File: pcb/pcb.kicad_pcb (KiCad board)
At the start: 2 copper layers, 156.4 x 127.2 mm, 67 parts, among them SW1 SW_Push, SW10 SW_Push, SW11 SW_Push, SW12 SW_Push, SW13 SW_Push, SW14 SW_Push, SW15 SW_Push, SW16 SW_Push, SW17 SW_Push, SW18 SW_Push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

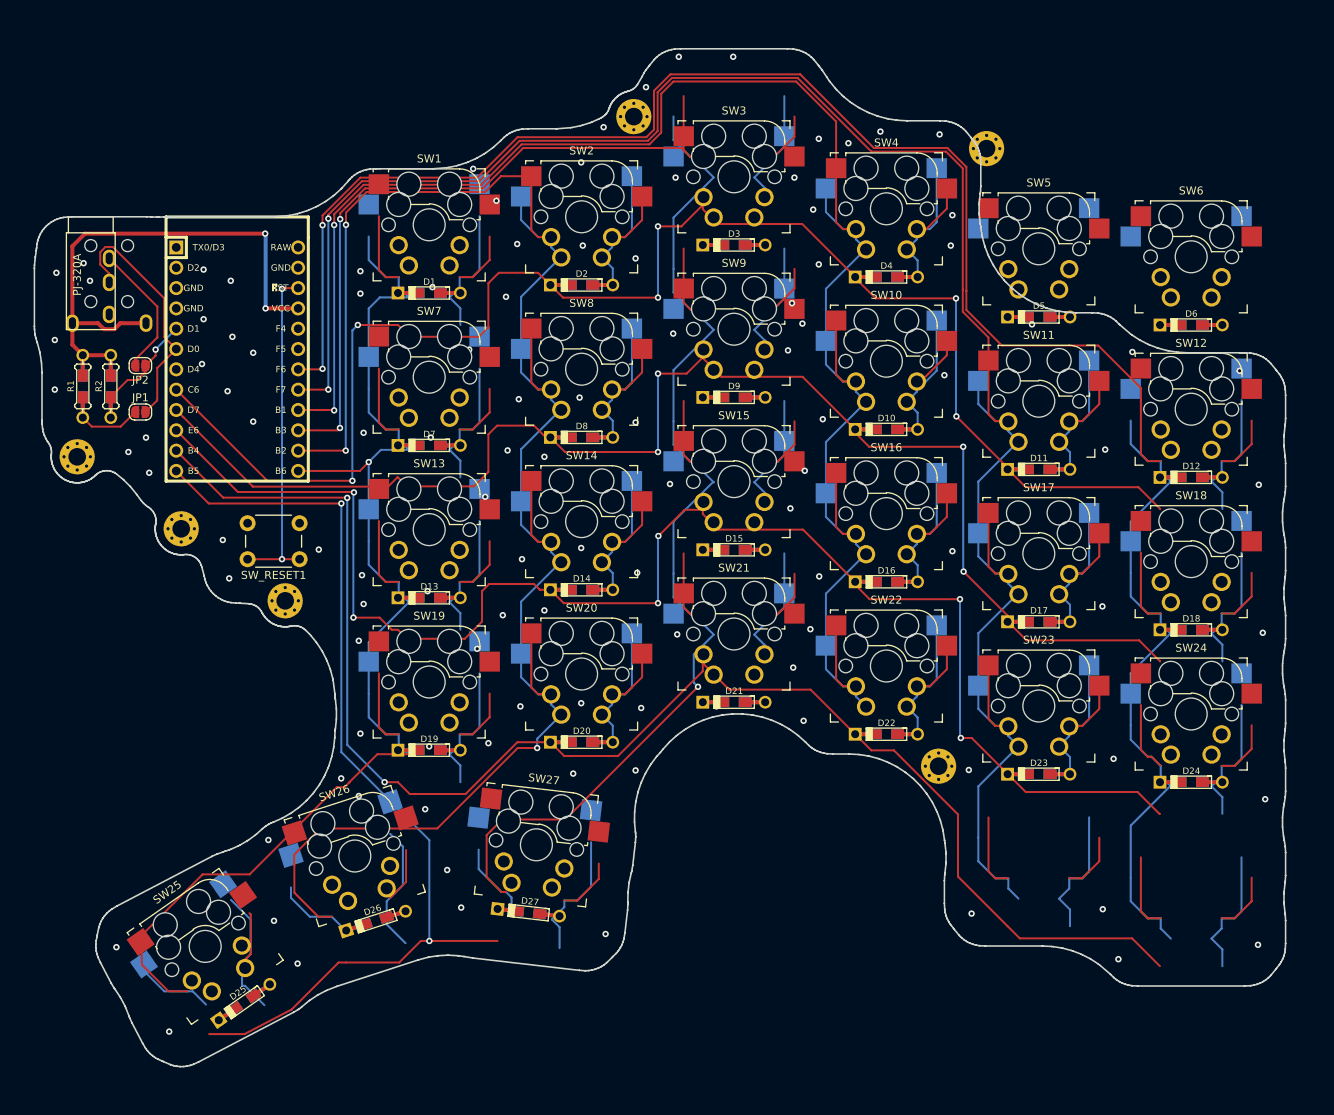
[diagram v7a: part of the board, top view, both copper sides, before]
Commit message: Route new switch placement
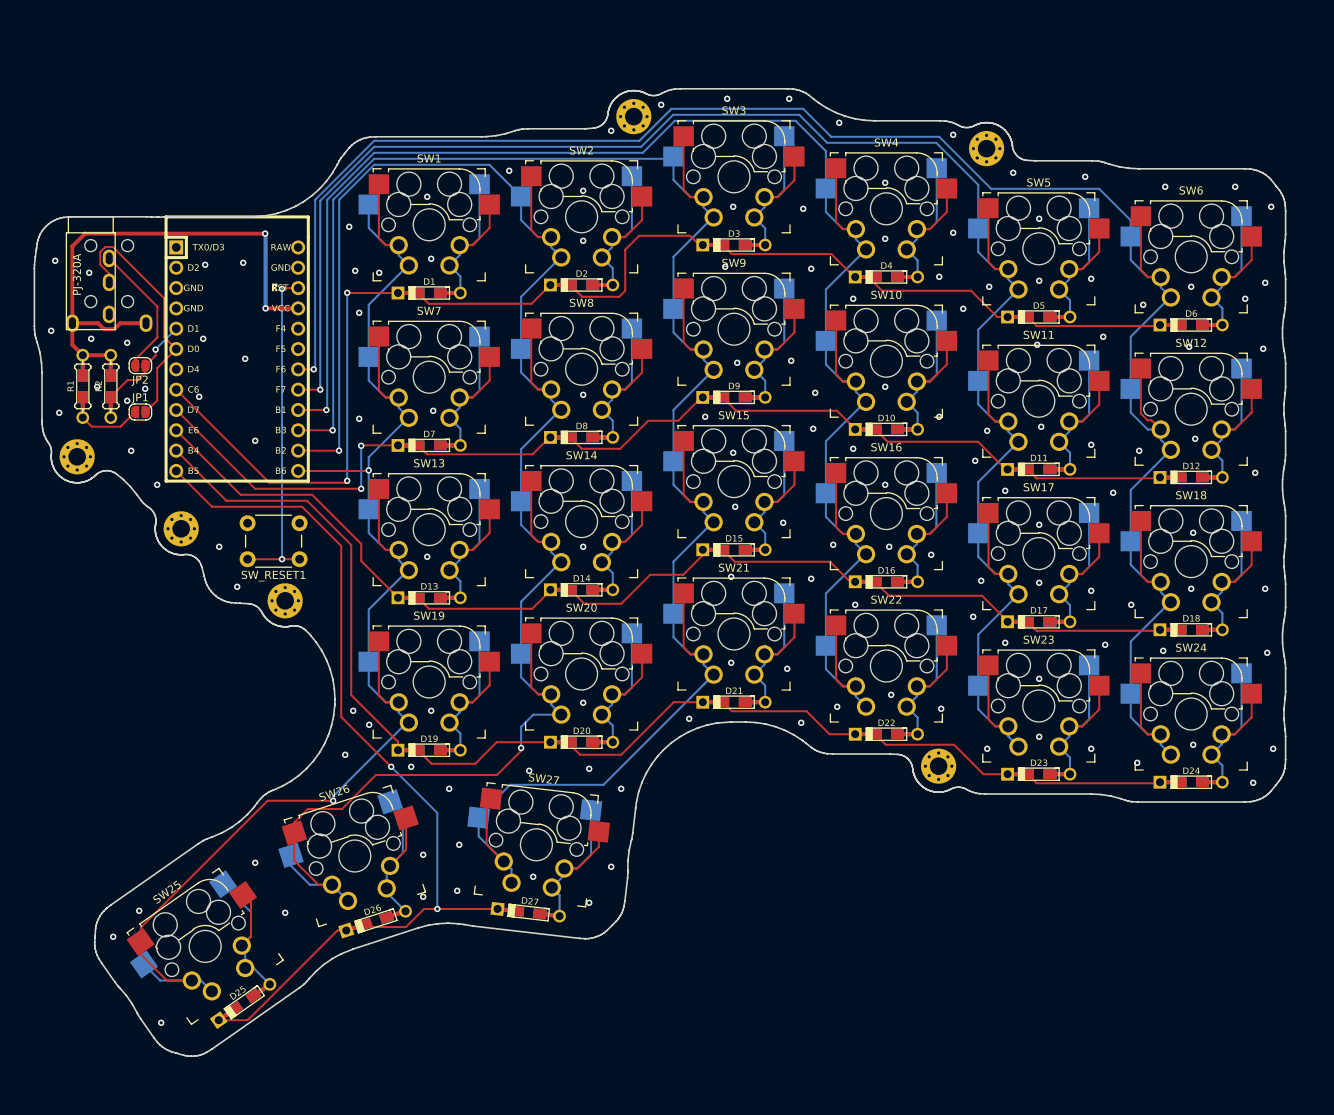
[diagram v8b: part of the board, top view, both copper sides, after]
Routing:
- net (no net): track 163.3 -> 0.00 mm, vias 1 -> 0
- net /col2: track 117.0 -> 255.3 mm, vias 2 -> 1
- net /row2: track 185.2 -> 130.2 mm, vias 6 -> 0
- net /row1: track 171.4 -> 129.4 mm, vias 4 -> 2
- net /row3: track 188.1 -> 147.2 mm, vias 2 -> 0
- net /row0: track 191.4 -> 152.5 mm, vias 6 -> 2
- net /row4: track 142.4 -> 114.1 mm
- net /col5: track 283.2 -> 258.6 mm, vias 2 -> 1
- net Net-(D5-Pad2): track 0.00 -> 24.2 mm
- net Net-(D23-Pad2): track 48.5 -> 24.2 mm
- net /col4: track 266.4 -> 243.7 mm, vias 2 -> 1
- net Net-(D24-Pad2): track 40.9 -> 24.2 mm
- net Net-(D6-Pad2): track 7.58 -> 24.2 mm
- net /col1: track 234.5 -> 246.0 mm, vias 3 -> 2
- net Net-(D21-Pad2): track 16.7 -> 26.3 mm
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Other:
- board size 156.4 x 127.2 mm -> 156.4 x 120.9 mm
